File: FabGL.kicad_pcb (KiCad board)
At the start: 2 copper layers, 65 x 56 mm, 32 parts, among them J2 Mini-DIN-6, J3 Mini-DIN-6, J6 DB15_Female_HighDensity, P1 2x40 2.54

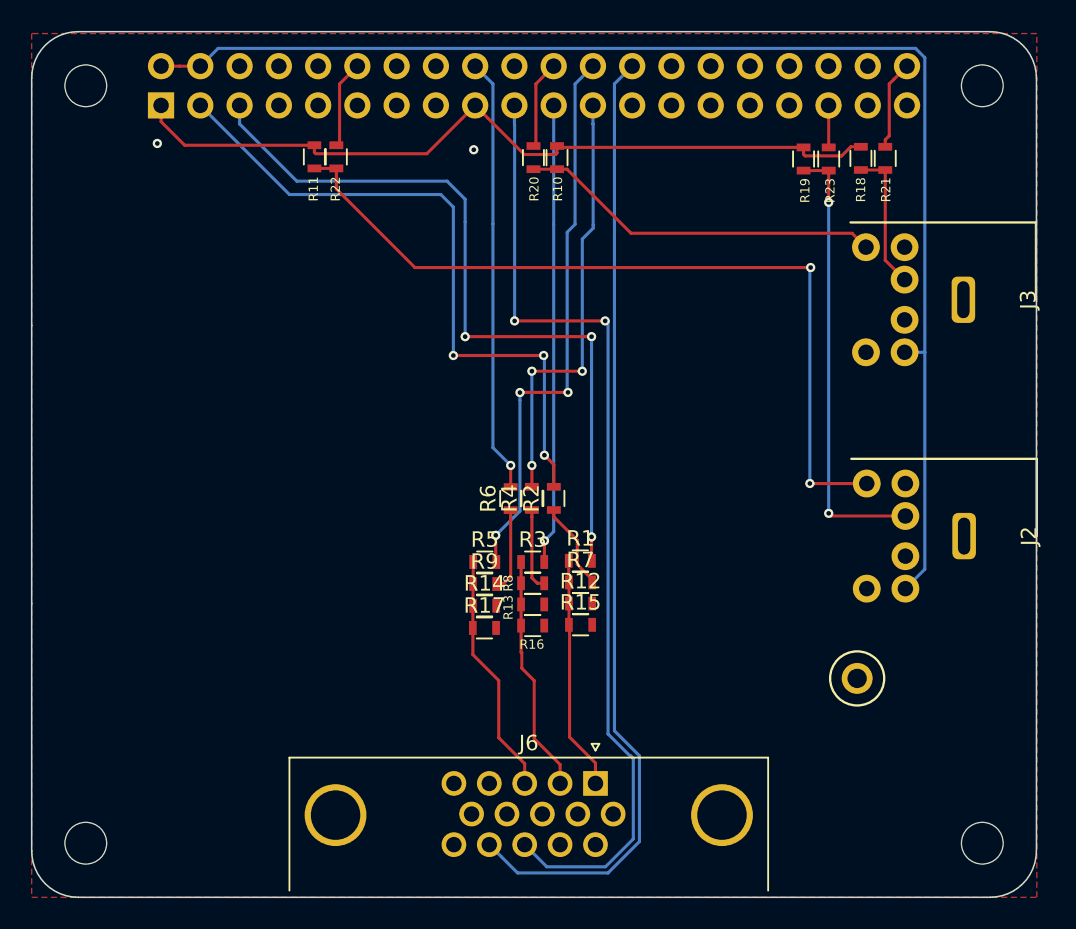
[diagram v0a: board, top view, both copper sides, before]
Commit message: License and PCB adjustments
Added CERN OHL 1.2
Added Proto Area for both DIP and SOIC
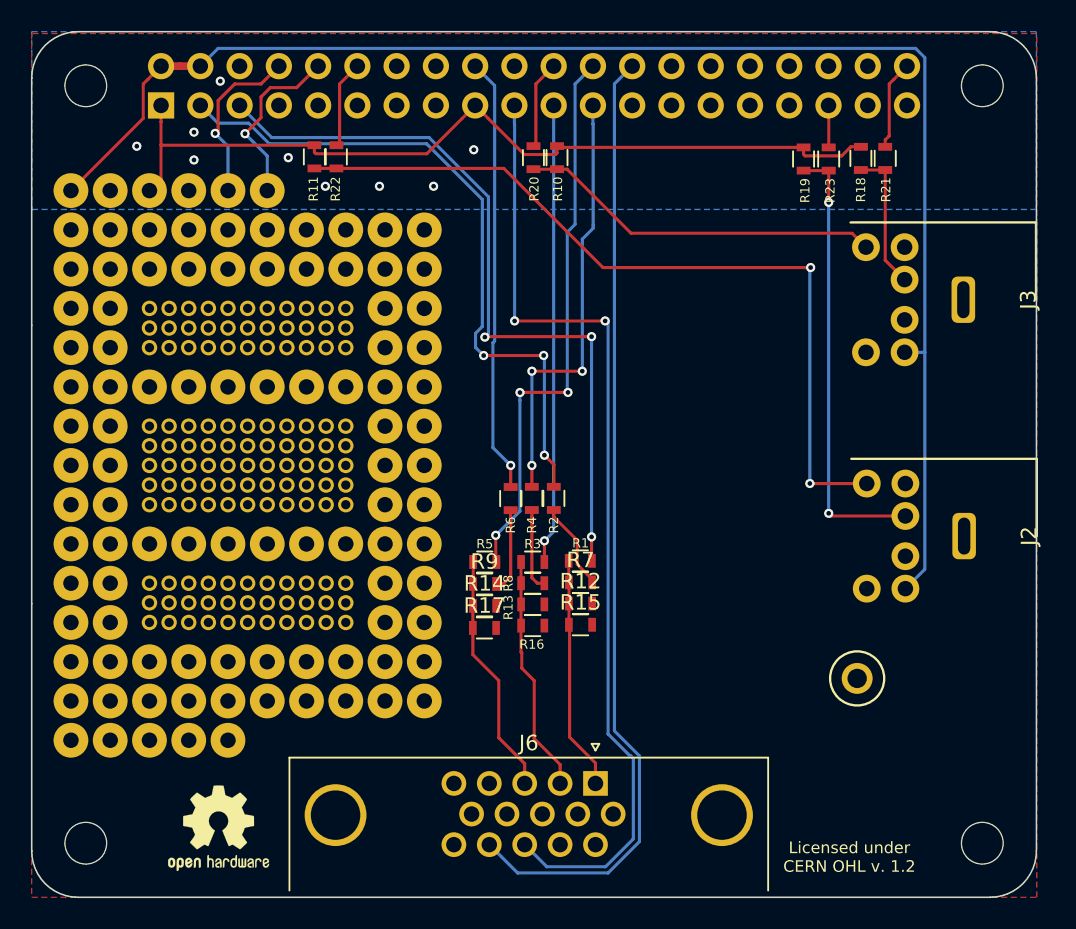
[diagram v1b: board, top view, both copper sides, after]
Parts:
- added REF**: SolderWirePad_1x01_Drill1mm, Connector_Wire:SolderWirePad_1x01_Drill1mm, F.Cu at (124.8, 65.9)
- added REF**: SolderWirePad_1x01_Drill1mm, Connector_Wire:SolderWirePad_1x01_Drill1mm, F.Cu at (135.0, 78.6)
- added REF**: SolderWirePad_1x01_Drill0.8mm, Connector_Wire:SolderWirePad_1x01_Drill0.8mm, F.Cu at (137.5, 74.8)
- added REF**: SolderWirePad_1x01_Drill0.8mm, Connector_Wire:SolderWirePad_1x01_Drill0.8mm, F.Cu at (132.4, 86.2)
- added REF**: SolderWirePad_1x01_Drill0.8mm, Connector_Wire:SolderWirePad_1x01_Drill0.8mm, F.Cu at (132.4, 84.9)
- added REF**: SolderWirePad_1x01_Drill0.8mm, Connector_Wire:SolderWirePad_1x01_Drill0.8mm, F.Cu at (132.4, 83.6)
- added REF**: SolderWirePad_1x01_Drill0.8mm, Connector_Wire:SolderWirePad_1x01_Drill0.8mm, F.Cu at (132.4, 82.4)
- added REF**: SolderWirePad_1x01_Drill0.8mm, Connector_Wire:SolderWirePad_1x01_Drill0.8mm, F.Cu at (132.4, 76.0)
- added REF**: SolderWirePad_1x01_Drill0.8mm, Connector_Wire:SolderWirePad_1x01_Drill0.8mm, F.Cu at (132.4, 74.8)
- added REF**: SolderWirePad_1x01_Drill0.8mm, Connector_Wire:SolderWirePad_1x01_Drill0.8mm, F.Cu at (136.2, 86.2)
- added REF**: SolderWirePad_1x01_Drill0.8mm, Connector_Wire:SolderWirePad_1x01_Drill0.8mm, F.Cu at (136.2, 84.9)
- added REF**: SolderWirePad_1x01_Drill0.8mm, Connector_Wire:SolderWirePad_1x01_Drill0.8mm, F.Cu at (136.2, 83.6)
- added REF**: SolderWirePad_1x01_Drill1mm, Connector_Wire:SolderWirePad_1x01_Drill1mm, F.Cu at (137.5, 78.6)
- added REF**: SolderWirePad_1x01_Drill0.8mm, Connector_Wire:SolderWirePad_1x01_Drill0.8mm, F.Cu at (136.2, 82.4)
- added REF**: SolderWirePad_1x01_Drill0.8mm, Connector_Wire:SolderWirePad_1x01_Drill0.8mm, F.Cu at (136.2, 76.0)
- added REF**: SolderWirePad_1x01_Drill0.8mm, Connector_Wire:SolderWirePad_1x01_Drill0.8mm, F.Cu at (136.2, 74.8)
- added REF**: SolderWirePad_1x01_Drill0.8mm, Connector_Wire:SolderWirePad_1x01_Drill0.8mm, F.Cu at (131.2, 86.2)
- added REF**: SolderWirePad_1x01_Drill0.8mm, Connector_Wire:SolderWirePad_1x01_Drill0.8mm, F.Cu at (131.2, 84.9)
- added REF**: SolderWirePad_1x01_Drill0.8mm, Connector_Wire:SolderWirePad_1x01_Drill0.8mm, F.Cu at (131.2, 83.6)
- added REF**: SolderWirePad_1x01_Drill0.8mm, Connector_Wire:SolderWirePad_1x01_Drill0.8mm, F.Cu at (131.2, 82.4)
- added REF**: SolderWirePad_1x01_Drill0.8mm, Connector_Wire:SolderWirePad_1x01_Drill0.8mm, F.Cu at (131.2, 76.0)
- added REF**: SolderWirePad_1x01_Drill0.8mm, Connector_Wire:SolderWirePad_1x01_Drill0.8mm, F.Cu at (131.2, 74.8)
- added REF**: SolderWirePad_1x01_Drill0.8mm, Connector_Wire:SolderWirePad_1x01_Drill0.8mm, F.Cu at (129.9, 86.2)
- added REF**: SolderWirePad_1x01_Drill1mm, Connector_Wire:SolderWirePad_1x01_Drill1mm, F.Cu at (140.1, 78.6)
- added REF**: SolderWirePad_1x01_Drill0.8mm, Connector_Wire:SolderWirePad_1x01_Drill0.8mm, F.Cu at (129.9, 84.9)
- added REF**: SolderWirePad_1x01_Drill0.8mm, Connector_Wire:SolderWirePad_1x01_Drill0.8mm, F.Cu at (129.9, 83.6)
- added REF**: SolderWirePad_1x01_Drill0.8mm, Connector_Wire:SolderWirePad_1x01_Drill0.8mm, F.Cu at (129.9, 82.4)
- added REF**: SolderWirePad_1x01_Drill0.8mm, Connector_Wire:SolderWirePad_1x01_Drill0.8mm, F.Cu at (129.9, 76.0)
- added REF**: SolderWirePad_1x01_Drill0.8mm, Connector_Wire:SolderWirePad_1x01_Drill0.8mm, F.Cu at (129.9, 74.8)
- added REF**: SolderWirePad_1x01_Drill0.8mm, Connector_Wire:SolderWirePad_1x01_Drill0.8mm, F.Cu at (133.7, 86.2)
- added REF**: SolderWirePad_1x01_Drill0.8mm, Connector_Wire:SolderWirePad_1x01_Drill0.8mm, F.Cu at (133.7, 84.9)
- added REF**: SolderWirePad_1x01_Drill0.8mm, Connector_Wire:SolderWirePad_1x01_Drill0.8mm, F.Cu at (133.7, 83.6)
- added REF**: SolderWirePad_1x01_Drill0.8mm, Connector_Wire:SolderWirePad_1x01_Drill0.8mm, F.Cu at (133.7, 82.4)
- added REF**: SolderWirePad_1x01_Drill0.8mm, Connector_Wire:SolderWirePad_1x01_Drill0.8mm, F.Cu at (133.7, 76.0)
- added REF**: SolderWirePad_1x01_Drill0.8mm, Connector_Wire:SolderWirePad_1x01_Drill0.8mm, F.Cu at (135.0, 81.1)
- added REF**: SolderWirePad_1x01_Drill0.8mm, Connector_Wire:SolderWirePad_1x01_Drill0.8mm, F.Cu at (133.7, 74.8)
- added REF**: SolderWirePad_1x01_Drill0.8mm, Connector_Wire:SolderWirePad_1x01_Drill0.8mm, F.Cu at (138.8, 73.5)
- added REF**: SolderWirePad_1x01_Drill0.8mm, Connector_Wire:SolderWirePad_1x01_Drill0.8mm, F.Cu at (140.1, 73.5)
- added REF**: SolderWirePad_1x01_Drill0.8mm, Connector_Wire:SolderWirePad_1x01_Drill0.8mm, F.Cu at (137.5, 73.5)
- added REF**: SolderWirePad_1x01_Drill0.8mm, Connector_Wire:SolderWirePad_1x01_Drill0.8mm, F.Cu at (132.4, 73.5)
- added REF**: SolderWirePad_1x01_Drill0.8mm, Connector_Wire:SolderWirePad_1x01_Drill0.8mm, F.Cu at (133.7, 73.5)
- added REF**: SolderWirePad_1x01_Drill0.8mm, Connector_Wire:SolderWirePad_1x01_Drill0.8mm, F.Cu at (136.2, 73.5)
- added REF**: SolderWirePad_1x01_Drill0.8mm, Connector_Wire:SolderWirePad_1x01_Drill0.8mm, F.Cu at (135.0, 73.5)
- added REF**: SolderWirePad_1x01_Drill0.8mm, Connector_Wire:SolderWirePad_1x01_Drill0.8mm, F.Cu at (131.2, 73.5)
- added REF**: SolderWirePad_1x01_Drill0.8mm, Connector_Wire:SolderWirePad_1x01_Drill0.8mm, F.Cu at (129.9, 73.5)
- added REF**: SolderWirePad_1x01_Drill0.8mm, Connector_Wire:SolderWirePad_1x01_Drill0.8mm, F.Cu at (128.6, 81.1)
- added REF**: SolderWirePad_1x01_Drill0.8mm, Connector_Wire:SolderWirePad_1x01_Drill0.8mm, F.Cu at (128.6, 73.5)
- added REF**: SolderWirePad_1x01_Drill0.8mm, Connector_Wire:SolderWirePad_1x01_Drill0.8mm, F.Cu at (127.4, 73.5)
- added REF**: SolderWirePad_1x01_Drill1mm, Connector_Wire:SolderWirePad_1x01_Drill1mm, F.Cu at (142.6, 93.8)
- added REF**: SolderWirePad_1x01_Drill1mm, Connector_Wire:SolderWirePad_1x01_Drill1mm, F.Cu at (124.8, 93.8)
- added REF**: SolderWirePad_1x01_Drill1mm, Connector_Wire:SolderWirePad_1x01_Drill1mm, F.Cu at (124.8, 73.5)
- added REF**: SolderWirePad_1x01_Drill1mm, Connector_Wire:SolderWirePad_1x01_Drill1mm, F.Cu at (142.6, 73.5)
- added REF**: SolderWirePad_1x01_Drill1mm, Connector_Wire:SolderWirePad_1x01_Drill1mm, F.Cu at (142.6, 83.6)
- added REF**: SolderWirePad_1x01_Drill1mm, Connector_Wire:SolderWirePad_1x01_Drill1mm, F.Cu at (142.6, 78.6)
- added REF**: SolderWirePad_1x01_Drill1mm, Connector_Wire:SolderWirePad_1x01_Drill1mm, F.Cu at (142.6, 76.0)
- added REF**: SolderWirePad_1x01_Drill1mm, Connector_Wire:SolderWirePad_1x01_Drill1mm, F.Cu at (142.6, 86.2)
- added REF**: SolderWirePad_1x01_Drill0.8mm, Connector_Wire:SolderWirePad_1x01_Drill0.8mm, F.Cu at (127.4, 81.1)
- added REF**: SolderWirePad_1x01_Drill1mm, Connector_Wire:SolderWirePad_1x01_Drill1mm, F.Cu at (142.6, 91.3)
- added REF**: SolderWirePad_1x01_Drill1mm, Connector_Wire:SolderWirePad_1x01_Drill1mm, F.Cu at (142.6, 81.1)
- added REF**: SolderWirePad_1x01_Drill1mm, Connector_Wire:SolderWirePad_1x01_Drill1mm, F.Cu at (124.8, 91.3)
- added REF**: SolderWirePad_1x01_Drill1mm, Connector_Wire:SolderWirePad_1x01_Drill1mm, F.Cu at (124.8, 78.6)
- added REF**: SolderWirePad_1x01_Drill1mm, Connector_Wire:SolderWirePad_1x01_Drill1mm, F.Cu at (124.8, 86.2)
- added REF**: SolderWirePad_1x01_Drill1mm, Connector_Wire:SolderWirePad_1x01_Drill1mm, F.Cu at (124.8, 83.6)
- added REF**: SolderWirePad_1x01_Drill1mm, Connector_Wire:SolderWirePad_1x01_Drill1mm, F.Cu at (124.8, 76.0)
- added REF**: SolderWirePad_1x01_Drill1mm, Connector_Wire:SolderWirePad_1x01_Drill1mm, F.Cu at (124.8, 81.1)
- added REF**: SolderWirePad_1x01_Drill1mm, Connector_Wire:SolderWirePad_1x01_Drill1mm, F.Cu at (129.9, 96.3)
- added REF**: SolderWirePad_1x01_Drill1mm, Connector_Wire:SolderWirePad_1x01_Drill1mm, F.Cu at (124.8, 96.3)
- added REF**: SolderWirePad_1x01_Drill0.8mm, Connector_Wire:SolderWirePad_1x01_Drill0.8mm, F.Cu at (138.8, 81.1)
- added REF**: SolderWirePad_1x01_Drill1mm, Connector_Wire:SolderWirePad_1x01_Drill1mm, F.Cu at (127.4, 96.3)
- added REF**: SolderWirePad_1x01_Drill1mm, Connector_Wire:SolderWirePad_1x01_Drill1mm, F.Cu at (142.6, 96.3)
- added REF**: SolderWirePad_1x01_Drill1mm, Connector_Wire:SolderWirePad_1x01_Drill1mm, F.Cu at (137.5, 96.3)
- added REF**: SolderWirePad_1x01_Drill1mm, Connector_Wire:SolderWirePad_1x01_Drill1mm, F.Cu at (132.4, 96.3)
- added REF**: SolderWirePad_1x01_Drill1mm, Connector_Wire:SolderWirePad_1x01_Drill1mm, F.Cu at (140.1, 96.3)
- added REF**: SolderWirePad_1x01_Drill1mm, Connector_Wire:SolderWirePad_1x01_Drill1mm, F.Cu at (135.0, 96.3)
- added REF**: SolderWirePad_1x01_Drill1mm, Connector_Wire:SolderWirePad_1x01_Drill1mm, F.Cu at (140.1, 70.9)
- added REF**: SolderWirePad_1x01_Drill1mm, Connector_Wire:SolderWirePad_1x01_Drill1mm, F.Cu at (124.8, 70.9)
- added REF**: SolderWirePad_1x01_Drill1mm, Connector_Wire:SolderWirePad_1x01_Drill1mm, F.Cu at (132.4, 70.9)
- added REF**: SolderWirePad_1x01_Drill1mm, Connector_Wire:SolderWirePad_1x01_Drill1mm, F.Cu at (129.9, 70.9)
- added REF**: SolderWirePad_1x01_Drill0.8mm, Connector_Wire:SolderWirePad_1x01_Drill0.8mm, F.Cu at (137.5, 81.1)
- added REF**: SolderWirePad_1x01_Drill1mm, Connector_Wire:SolderWirePad_1x01_Drill1mm, F.Cu at (135.0, 70.9)
- added REF**: SolderWirePad_1x01_Drill1mm, Connector_Wire:SolderWirePad_1x01_Drill1mm, F.Cu at (142.6, 70.9)
- added REF**: SolderWirePad_1x01_Drill1mm, Connector_Wire:SolderWirePad_1x01_Drill1mm, F.Cu at (137.5, 70.9)
- added REF**: SolderWirePad_1x01_Drill1mm, Connector_Wire:SolderWirePad_1x01_Drill1mm, F.Cu at (127.4, 70.9)
- added REF**: SolderWirePad_1x01_Drill1mm, Connector_Wire:SolderWirePad_1x01_Drill1mm, F.Cu at (129.9, 98.9)
- added REF**: SolderWirePad_1x01_Drill1mm, Connector_Wire:SolderWirePad_1x01_Drill1mm, F.Cu at (124.8, 98.9)
- added REF**: SolderWirePad_1x01_Drill1mm, Connector_Wire:SolderWirePad_1x01_Drill1mm, F.Cu at (127.4, 98.9)
- added REF**: SolderWirePad_1x01_Drill1mm, Connector_Wire:SolderWirePad_1x01_Drill1mm, F.Cu at (145.1, 96.3)
- added REF**: SolderWirePad_1x01_Drill1mm, Connector_Wire:SolderWirePad_1x01_Drill1mm, F.Cu at (145.1, 93.8)
- added REF**: SolderWirePad_1x01_Drill1mm, Connector_Wire:SolderWirePad_1x01_Drill1mm, F.Cu at (145.1, 91.3)
- added REF**: SolderWirePad_1x01_Drill0.8mm, Connector_Wire:SolderWirePad_1x01_Drill0.8mm, F.Cu at (132.4, 81.1)
- added REF**: SolderWirePad_1x01_Drill1mm, Connector_Wire:SolderWirePad_1x01_Drill1mm, F.Cu at (145.1, 88.7)
- added REF**: SolderWirePad_1x01_Drill1mm, Connector_Wire:SolderWirePad_1x01_Drill1mm, F.Cu at (145.1, 86.2)
- added REF**: SolderWirePad_1x01_Drill1mm, Connector_Wire:SolderWirePad_1x01_Drill1mm, F.Cu at (145.1, 83.6)
- added REF**: SolderWirePad_1x01_Drill1mm, Connector_Wire:SolderWirePad_1x01_Drill1mm, F.Cu at (145.1, 81.1)
- added REF**: SolderWirePad_1x01_Drill1mm, Connector_Wire:SolderWirePad_1x01_Drill1mm, F.Cu at (145.1, 78.6)
- added REF**: SolderWirePad_1x01_Drill1mm, Connector_Wire:SolderWirePad_1x01_Drill1mm, F.Cu at (145.1, 76.0)
- added REF**: SolderWirePad_1x01_Drill1mm, Connector_Wire:SolderWirePad_1x01_Drill1mm, F.Cu at (145.1, 73.5)
- added REF**: SolderWirePad_1x01_Drill1mm, Connector_Wire:SolderWirePad_1x01_Drill1mm, F.Cu at (145.1, 70.9)
- added REF**: SolderWirePad_1x01_Drill1mm, Connector_Wire:SolderWirePad_1x01_Drill1mm, F.Cu at (145.1, 98.9)
- added REF**: SolderWirePad_1x01_Drill1mm, Connector_Wire:SolderWirePad_1x01_Drill1mm, F.Cu at (142.6, 98.9)
- added REF**: SolderWirePad_1x01_Drill0.8mm, Connector_Wire:SolderWirePad_1x01_Drill0.8mm, F.Cu at (136.2, 81.1)
- added REF**: SolderWirePad_1x01_Drill1mm, Connector_Wire:SolderWirePad_1x01_Drill1mm, F.Cu at (140.1, 98.9)
- added REF**: SolderWirePad_1x01_Drill1mm, Connector_Wire:SolderWirePad_1x01_Drill1mm, F.Cu at (137.5, 98.9)
- added REF**: SolderWirePad_1x01_Drill1mm, Connector_Wire:SolderWirePad_1x01_Drill1mm, F.Cu at (135.0, 98.9)
- added REF**: SolderWirePad_1x01_Drill1mm, Connector_Wire:SolderWirePad_1x01_Drill1mm, F.Cu at (132.4, 98.9)
- added REF**: SolderWirePad_1x01_Drill1mm, Connector_Wire:SolderWirePad_1x01_Drill1mm, F.Cu at (132.4, 101.4)
- added REF**: SolderWirePad_1x01_Drill1mm, Connector_Wire:SolderWirePad_1x01_Drill1mm, F.Cu at (129.9, 101.4)
- added REF**: SolderWirePad_1x01_Drill1mm, Connector_Wire:SolderWirePad_1x01_Drill1mm, F.Cu at (127.4, 101.4)
- added REF**: SolderWirePad_1x01_Drill1mm, Connector_Wire:SolderWirePad_1x01_Drill1mm, F.Cu at (124.8, 101.4)
- added REF**: SolderWirePad_1x01_Drill1mm, Connector_Wire:SolderWirePad_1x01_Drill1mm, F.Cu at (122.3, 101.4)
- added REF**: SolderWirePad_1x01_Drill1mm, Connector_Wire:SolderWirePad_1x01_Drill1mm, F.Cu at (122.3, 98.9)
- added REF**: SolderWirePad_1x01_Drill1mm, Connector_Wire:SolderWirePad_1x01_Drill1mm, F.Cu at (132.4, 65.9)
- added REF**: SolderWirePad_1x01_Drill0.8mm, Connector_Wire:SolderWirePad_1x01_Drill0.8mm, F.Cu at (131.2, 81.1)
- added REF**: SolderWirePad_1x01_Drill1mm, Connector_Wire:SolderWirePad_1x01_Drill1mm, F.Cu at (122.3, 96.3)
- added REF**: SolderWirePad_1x01_Drill1mm, Connector_Wire:SolderWirePad_1x01_Drill1mm, F.Cu at (122.3, 93.8)
- added REF**: SolderWirePad_1x01_Drill1mm, Connector_Wire:SolderWirePad_1x01_Drill1mm, F.Cu at (122.3, 91.3)
- added REF**: SolderWirePad_1x01_Drill1mm, Connector_Wire:SolderWirePad_1x01_Drill1mm, F.Cu at (122.3, 88.7)
- added REF**: SolderWirePad_1x01_Drill1mm, Connector_Wire:SolderWirePad_1x01_Drill1mm, F.Cu at (122.3, 86.2)
- added REF**: SolderWirePad_1x01_Drill1mm, Connector_Wire:SolderWirePad_1x01_Drill1mm, F.Cu at (122.3, 83.6)
- added REF**: SolderWirePad_1x01_Drill1mm, Connector_Wire:SolderWirePad_1x01_Drill1mm, F.Cu at (122.3, 81.1)
- added REF**: SolderWirePad_1x01_Drill1mm, Connector_Wire:SolderWirePad_1x01_Drill1mm, F.Cu at (122.3, 78.6)
- added REF**: SolderWirePad_1x01_Drill1mm, Connector_Wire:SolderWirePad_1x01_Drill1mm, F.Cu at (122.3, 76.0)
- added REF**: SolderWirePad_1x01_Drill1mm, Connector_Wire:SolderWirePad_1x01_Drill1mm, F.Cu at (122.3, 73.5)
- added REF**: SolderWirePad_1x01_Drill0.8mm, Connector_Wire:SolderWirePad_1x01_Drill0.8mm, F.Cu at (129.9, 81.1)
- added REF**: SolderWirePad_1x01_Drill1mm, Connector_Wire:SolderWirePad_1x01_Drill1mm, F.Cu at (122.3, 70.9)
- added REF**: SolderWirePad_1x01_Drill1mm, Connector_Wire:SolderWirePad_1x01_Drill1mm, F.Cu at (145.1, 68.4)
- added REF**: SolderWirePad_1x01_Drill1mm, Connector_Wire:SolderWirePad_1x01_Drill1mm, F.Cu at (142.6, 68.4)
- added REF**: SolderWirePad_1x01_Drill1mm, Connector_Wire:SolderWirePad_1x01_Drill1mm, F.Cu at (140.1, 68.4)
- added REF**: SolderWirePad_1x01_Drill1mm, Connector_Wire:SolderWirePad_1x01_Drill1mm, F.Cu at (137.5, 68.4)
- added REF**: SolderWirePad_1x01_Drill1mm, Connector_Wire:SolderWirePad_1x01_Drill1mm, F.Cu at (135.0, 68.4)
- added REF**: SolderWirePad_1x01_Drill1mm, Connector_Wire:SolderWirePad_1x01_Drill1mm, F.Cu at (132.4, 68.4)
- added REF**: SolderWirePad_1x01_Drill1mm, Connector_Wire:SolderWirePad_1x01_Drill1mm, F.Cu at (129.9, 68.4)
- added REF**: SolderWirePad_1x01_Drill1mm, Connector_Wire:SolderWirePad_1x01_Drill1mm, F.Cu at (127.4, 68.4)
- added REF**: SolderWirePad_1x01_Drill1mm, Connector_Wire:SolderWirePad_1x01_Drill1mm, F.Cu at (124.8, 68.4)
- added REF**: SolderWirePad_1x01_Drill0.8mm, Connector_Wire:SolderWirePad_1x01_Drill0.8mm, F.Cu at (133.7, 81.1)
- added REF**: SolderWirePad_1x01_Drill1mm, Connector_Wire:SolderWirePad_1x01_Drill1mm, F.Cu at (122.3, 68.4)
- added REF**: KiCad-Logo2_5mm_SilkScreen, Symbol:KiCad-Logo2_5mm_SilkScreen, B.Cu at (180.5, 97.0)
- added REF**: OSHW-Logo2_7.3x6mm_SilkScreen, Symbol:OSHW-Logo2_7.3x6mm_SilkScreen, F.Cu at (131.8, 107.1)
- added REF**: SolderWirePad_1x01_Drill0.8mm, Connector_Wire:SolderWirePad_1x01_Drill0.8mm, F.Cu at (129.9, 91.3)
- added REF**: SolderWirePad_1x01_Drill0.8mm, Connector_Wire:SolderWirePad_1x01_Drill0.8mm, F.Cu at (131.2, 91.3)
- added REF**: SolderWirePad_1x01_Drill0.8mm, Connector_Wire:SolderWirePad_1x01_Drill0.8mm, F.Cu at (133.7, 91.3)
- added REF**: SolderWirePad_1x01_Drill0.8mm, Connector_Wire:SolderWirePad_1x01_Drill0.8mm, F.Cu at (136.2, 91.3)
- added REF**: SolderWirePad_1x01_Drill0.8mm, Connector_Wire:SolderWirePad_1x01_Drill0.8mm, F.Cu at (135.0, 91.3)
- added REF**: SolderWirePad_1x01_Drill0.8mm, Connector_Wire:SolderWirePad_1x01_Drill0.8mm, F.Cu at (127.4, 91.3)
- added REF**: SolderWirePad_1x01_Drill0.8mm, Connector_Wire:SolderWirePad_1x01_Drill0.8mm, F.Cu at (128.6, 91.3)
- added REF**: SolderWirePad_1x01_Drill1mm, Connector_Wire:SolderWirePad_1x01_Drill1mm, F.Cu at (129.9, 65.9)
- added REF**: SolderWirePad_1x01_Drill0.8mm, Connector_Wire:SolderWirePad_1x01_Drill0.8mm, F.Cu at (132.4, 91.3)
- added REF**: SolderWirePad_1x01_Drill0.8mm, Connector_Wire:SolderWirePad_1x01_Drill0.8mm, F.Cu at (140.1, 91.3)
- added REF**: SolderWirePad_1x01_Drill0.8mm, Connector_Wire:SolderWirePad_1x01_Drill0.8mm, F.Cu at (137.5, 91.3)
- added REF**: SolderWirePad_1x01_Drill0.8mm, Connector_Wire:SolderWirePad_1x01_Drill0.8mm, F.Cu at (138.8, 91.3)
- added REF**: SolderWirePad_1x01_Drill1mm, Connector_Wire:SolderWirePad_1x01_Drill1mm, F.Cu at (129.9, 88.7)
- added REF**: SolderWirePad_1x01_Drill1mm, Connector_Wire:SolderWirePad_1x01_Drill1mm, F.Cu at (127.4, 88.7)
- added REF**: SolderWirePad_1x01_Drill1mm, Connector_Wire:SolderWirePad_1x01_Drill1mm, F.Cu at (137.5, 88.7)
- added REF**: SolderWirePad_1x01_Drill1mm, Connector_Wire:SolderWirePad_1x01_Drill1mm, F.Cu at (124.8, 88.7)
- added REF**: SolderWirePad_1x01_Drill1mm, Connector_Wire:SolderWirePad_1x01_Drill1mm, F.Cu at (142.6, 88.7)
- added REF**: SolderWirePad_1x01_Drill1mm, Connector_Wire:SolderWirePad_1x01_Drill1mm, F.Cu at (135.0, 88.7)
- added REF**: SolderWirePad_1x01_Drill1mm, Connector_Wire:SolderWirePad_1x01_Drill1mm, F.Cu at (135.0, 65.9)
- added REF**: SolderWirePad_1x01_Drill1mm, Connector_Wire:SolderWirePad_1x01_Drill1mm, F.Cu at (140.1, 88.7)
- added REF**: SolderWirePad_1x01_Drill1mm, Connector_Wire:SolderWirePad_1x01_Drill1mm, F.Cu at (132.4, 88.7)
- added REF**: SolderWirePad_1x01_Drill0.8mm, Connector_Wire:SolderWirePad_1x01_Drill0.8mm, F.Cu at (135.0, 93.8)
- added REF**: SolderWirePad_1x01_Drill0.8mm, Connector_Wire:SolderWirePad_1x01_Drill0.8mm, F.Cu at (135.0, 92.5)
- added REF**: SolderWirePad_1x01_Drill0.8mm, Connector_Wire:SolderWirePad_1x01_Drill0.8mm, F.Cu at (140.1, 93.8)
- added REF**: SolderWirePad_1x01_Drill0.8mm, Connector_Wire:SolderWirePad_1x01_Drill0.8mm, F.Cu at (140.1, 92.5)
- added REF**: SolderWirePad_1x01_Drill0.8mm, Connector_Wire:SolderWirePad_1x01_Drill0.8mm, F.Cu at (127.4, 93.8)
- added REF**: SolderWirePad_1x01_Drill0.8mm, Connector_Wire:SolderWirePad_1x01_Drill0.8mm, F.Cu at (127.4, 92.5)
- added REF**: SolderWirePad_1x01_Drill0.8mm, Connector_Wire:SolderWirePad_1x01_Drill0.8mm, F.Cu at (128.6, 93.8)
- added REF**: SolderWirePad_1x01_Drill0.8mm, Connector_Wire:SolderWirePad_1x01_Drill0.8mm, F.Cu at (128.6, 92.5)
- added REF**: SolderWirePad_1x01_Drill1mm, Connector_Wire:SolderWirePad_1x01_Drill1mm, F.Cu at (127.4, 65.9)
- added REF**: SolderWirePad_1x01_Drill0.8mm, Connector_Wire:SolderWirePad_1x01_Drill0.8mm, F.Cu at (137.5, 93.8)
- added REF**: SolderWirePad_1x01_Drill0.8mm, Connector_Wire:SolderWirePad_1x01_Drill0.8mm, F.Cu at (137.5, 92.5)
- added REF**: SolderWirePad_1x01_Drill0.8mm, Connector_Wire:SolderWirePad_1x01_Drill0.8mm, F.Cu at (138.8, 93.8)
- added REF**: SolderWirePad_1x01_Drill0.8mm, Connector_Wire:SolderWirePad_1x01_Drill0.8mm, F.Cu at (138.8, 92.5)
- added REF**: SolderWirePad_1x01_Drill0.8mm, Connector_Wire:SolderWirePad_1x01_Drill0.8mm, F.Cu at (132.4, 93.8)
- added REF**: SolderWirePad_1x01_Drill0.8mm, Connector_Wire:SolderWirePad_1x01_Drill0.8mm, F.Cu at (132.4, 92.5)
- added REF**: SolderWirePad_1x01_Drill0.8mm, Connector_Wire:SolderWirePad_1x01_Drill0.8mm, F.Cu at (131.2, 93.8)
- added REF**: SolderWirePad_1x01_Drill0.8mm, Connector_Wire:SolderWirePad_1x01_Drill0.8mm, F.Cu at (131.2, 92.5)
- added REF**: SolderWirePad_1x01_Drill0.8mm, Connector_Wire:SolderWirePad_1x01_Drill0.8mm, F.Cu at (136.2, 93.8)
- added REF**: SolderWirePad_1x01_Drill0.8mm, Connector_Wire:SolderWirePad_1x01_Drill0.8mm, F.Cu at (136.2, 92.5)
- added REF**: SolderWirePad_1x01_Drill1mm, Connector_Wire:SolderWirePad_1x01_Drill1mm, F.Cu at (122.3, 65.9)
- added REF**: SolderWirePad_1x01_Drill0.8mm, Connector_Wire:SolderWirePad_1x01_Drill0.8mm, F.Cu at (129.9, 93.8)
- added REF**: SolderWirePad_1x01_Drill0.8mm, Connector_Wire:SolderWirePad_1x01_Drill0.8mm, F.Cu at (129.9, 92.5)
- added REF**: SolderWirePad_1x01_Drill0.8mm, Connector_Wire:SolderWirePad_1x01_Drill0.8mm, F.Cu at (133.7, 93.8)
- added REF**: SolderWirePad_1x01_Drill0.8mm, Connector_Wire:SolderWirePad_1x01_Drill0.8mm, F.Cu at (133.7, 92.5)
- added REF**: SolderWirePad_1x01_Drill0.8mm, Connector_Wire:SolderWirePad_1x01_Drill0.8mm, F.Cu at (135.0, 86.2)
- added REF**: SolderWirePad_1x01_Drill0.8mm, Connector_Wire:SolderWirePad_1x01_Drill0.8mm, F.Cu at (135.0, 84.9)
- added REF**: SolderWirePad_1x01_Drill0.8mm, Connector_Wire:SolderWirePad_1x01_Drill0.8mm, F.Cu at (135.0, 83.6)
- added REF**: SolderWirePad_1x01_Drill0.8mm, Connector_Wire:SolderWirePad_1x01_Drill0.8mm, F.Cu at (135.0, 82.4)
- added REF**: SolderWirePad_1x01_Drill0.8mm, Connector_Wire:SolderWirePad_1x01_Drill0.8mm, F.Cu at (135.0, 76.0)
- added REF**: SolderWirePad_1x01_Drill0.8mm, Connector_Wire:SolderWirePad_1x01_Drill0.8mm, F.Cu at (135.0, 74.8)
- added REF**: SolderWirePad_1x01_Drill1mm, Connector_Wire:SolderWirePad_1x01_Drill1mm, F.Cu at (127.4, 78.6)
- added REF**: SolderWirePad_1x01_Drill0.8mm, Connector_Wire:SolderWirePad_1x01_Drill0.8mm, F.Cu at (140.1, 86.2)
- added REF**: SolderWirePad_1x01_Drill0.8mm, Connector_Wire:SolderWirePad_1x01_Drill0.8mm, F.Cu at (140.1, 84.9)
- added REF**: SolderWirePad_1x01_Drill0.8mm, Connector_Wire:SolderWirePad_1x01_Drill0.8mm, F.Cu at (140.1, 83.6)
- added REF**: SolderWirePad_1x01_Drill0.8mm, Connector_Wire:SolderWirePad_1x01_Drill0.8mm, F.Cu at (140.1, 82.4)
- added REF**: SolderWirePad_1x01_Drill0.8mm, Connector_Wire:SolderWirePad_1x01_Drill0.8mm, F.Cu at (140.1, 81.1)
- added REF**: SolderWirePad_1x01_Drill0.8mm, Connector_Wire:SolderWirePad_1x01_Drill0.8mm, F.Cu at (140.1, 76.0)
- added REF**: SolderWirePad_1x01_Drill0.8mm, Connector_Wire:SolderWirePad_1x01_Drill0.8mm, F.Cu at (140.1, 74.8)
- added REF**: SolderWirePad_1x01_Drill0.8mm, Connector_Wire:SolderWirePad_1x01_Drill0.8mm, F.Cu at (127.4, 86.2)
- added REF**: SolderWirePad_1x01_Drill0.8mm, Connector_Wire:SolderWirePad_1x01_Drill0.8mm, F.Cu at (127.4, 84.9)
- added REF**: SolderWirePad_1x01_Drill0.8mm, Connector_Wire:SolderWirePad_1x01_Drill0.8mm, F.Cu at (127.4, 83.6)
- added REF**: SolderWirePad_1x01_Drill1mm, Connector_Wire:SolderWirePad_1x01_Drill1mm, F.Cu at (129.9, 78.6)
- added REF**: SolderWirePad_1x01_Drill0.8mm, Connector_Wire:SolderWirePad_1x01_Drill0.8mm, F.Cu at (127.4, 82.4)
- added REF**: SolderWirePad_1x01_Drill0.8mm, Connector_Wire:SolderWirePad_1x01_Drill0.8mm, F.Cu at (127.4, 76.0)
- added REF**: SolderWirePad_1x01_Drill0.8mm, Connector_Wire:SolderWirePad_1x01_Drill0.8mm, F.Cu at (127.4, 74.8)
- added REF**: SolderWirePad_1x01_Drill0.8mm, Connector_Wire:SolderWirePad_1x01_Drill0.8mm, F.Cu at (128.6, 86.2)
- added REF**: SolderWirePad_1x01_Drill0.8mm, Connector_Wire:SolderWirePad_1x01_Drill0.8mm, F.Cu at (128.6, 84.9)
- added REF**: SolderWirePad_1x01_Drill0.8mm, Connector_Wire:SolderWirePad_1x01_Drill0.8mm, F.Cu at (128.6, 83.6)
- added REF**: SolderWirePad_1x01_Drill0.8mm, Connector_Wire:SolderWirePad_1x01_Drill0.8mm, F.Cu at (128.6, 82.4)
- added REF**: SolderWirePad_1x01_Drill0.8mm, Connector_Wire:SolderWirePad_1x01_Drill0.8mm, F.Cu at (128.6, 76.0)
- added REF**: SolderWirePad_1x01_Drill0.8mm, Connector_Wire:SolderWirePad_1x01_Drill0.8mm, F.Cu at (128.6, 74.8)
- added REF**: SolderWirePad_1x01_Drill0.8mm, Connector_Wire:SolderWirePad_1x01_Drill0.8mm, F.Cu at (138.8, 86.2)
- added REF**: SolderWirePad_1x01_Drill1mm, Connector_Wire:SolderWirePad_1x01_Drill1mm, F.Cu at (132.4, 78.6)
- added REF**: SolderWirePad_1x01_Drill0.8mm, Connector_Wire:SolderWirePad_1x01_Drill0.8mm, F.Cu at (138.8, 84.9)
- added REF**: SolderWirePad_1x01_Drill0.8mm, Connector_Wire:SolderWirePad_1x01_Drill0.8mm, F.Cu at (138.8, 83.6)
- added REF**: SolderWirePad_1x01_Drill0.8mm, Connector_Wire:SolderWirePad_1x01_Drill0.8mm, F.Cu at (138.8, 82.4)
- added REF**: SolderWirePad_1x01_Drill0.8mm, Connector_Wire:SolderWirePad_1x01_Drill0.8mm, F.Cu at (138.8, 76.0)
- added REF**: SolderWirePad_1x01_Drill0.8mm, Connector_Wire:SolderWirePad_1x01_Drill0.8mm, F.Cu at (138.8, 74.8)
- added REF**: SolderWirePad_1x01_Drill0.8mm, Connector_Wire:SolderWirePad_1x01_Drill0.8mm, F.Cu at (137.5, 86.2)
- added REF**: SolderWirePad_1x01_Drill0.8mm, Connector_Wire:SolderWirePad_1x01_Drill0.8mm, F.Cu at (137.5, 84.9)
- added REF**: SolderWirePad_1x01_Drill0.8mm, Connector_Wire:SolderWirePad_1x01_Drill0.8mm, F.Cu at (137.5, 83.6)
- added REF**: SolderWirePad_1x01_Drill0.8mm, Connector_Wire:SolderWirePad_1x01_Drill0.8mm, F.Cu at (137.5, 82.4)
- added REF**: SolderWirePad_1x01_Drill0.8mm, Connector_Wire:SolderWirePad_1x01_Drill0.8mm, F.Cu at (137.5, 76.0)
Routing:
- net /RXD: track 0.16 -> 11.8 mm, vias 0 -> 1
- net /TXD: track 0.15 -> 11.2 mm, vias 0 -> 1
- net +5V: track 86.7 -> 97.2 mm
- net +3.3VP: track 52.0 -> 56.2 mm
- net Net-(J2-Pad5): track 53.2 -> 52.4 mm
- net RED_LSB: track 43.3 -> 43.9 mm
- net GND: vias 2 -> 9
- added copper zone on B.Cu, net GND
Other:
- board text added: "Licensed under CERN OHL v. 1.2"
- board text added: "Revision History 2019-07-16: Initial commit, rough design 2019-07-17: Added proto area for DIP and SOIC"
- board text added: "https://github.com/singleboardsolutions http://singleboardsolutions.com Revision 2019.07.17"
- board text removed: "Revision History v1.0 - Initial template"
